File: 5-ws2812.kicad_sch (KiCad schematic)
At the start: 5 parts

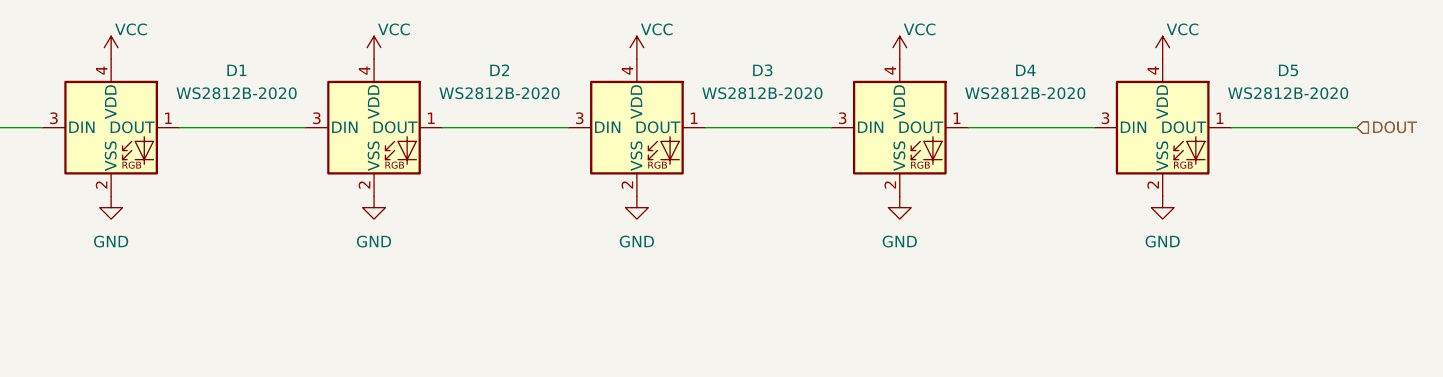
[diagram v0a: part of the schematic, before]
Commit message: Added front artwork and token on the back
Also:
- Tweaked the trace to the antenna to hopefully better match 50ohm impedance
- Tweaked all traces to use fillet on all corners
- Added/fixed parts information

Signed-off-by: Thomas Flummer <tf@flummer.net>
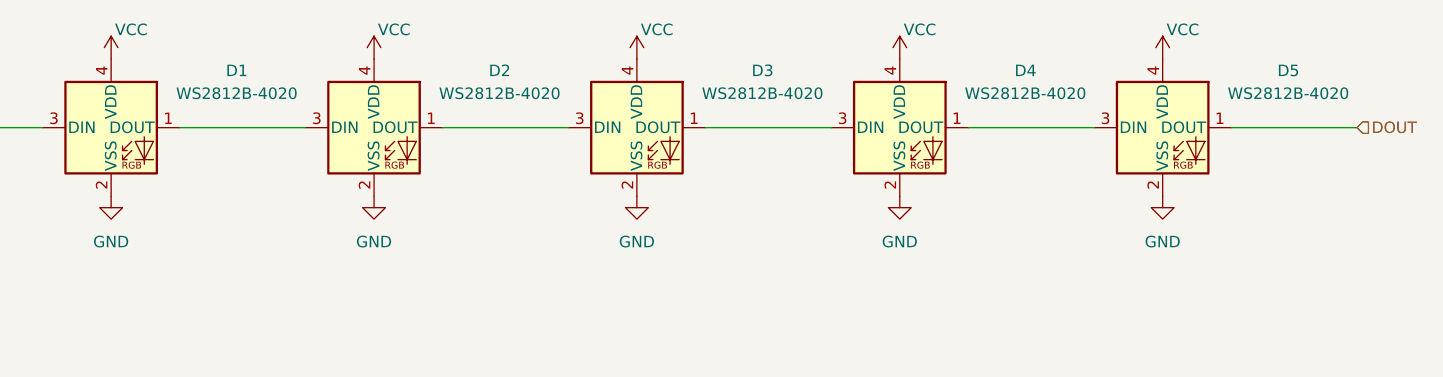
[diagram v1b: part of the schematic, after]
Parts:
- D1, D2, D3, D4, D5: value WS2812B-2020 -> WS2812B-4020; LCSC (none) -> C965557
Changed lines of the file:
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@@
 			)
 		)
-		(property "Value" "WS2812B-2020"
+		(property "Value" "WS2812B-4020"
 			(at 116.84 73.6914 0)
 			(effects
@@
 		)
 		(property "Description" "RGB LED with integrated controller, 2.0 x 2.0 mm, 12 mA"
+			(at 102.87 77.47 0)
+			(effects
+				(font
+					(size 1.27 1.27)
+				)
+				(hide yes)
+			)
+		)
+		(property "LCSC" "C965557"
 			(at 102.87 77.47 0)
 			(effects
@@
 			)
 		)
-		(property "Value" "WS2812B-2020"
+		(property "Value" "WS2812B-4020"
 			(at 175.26 73.6914 0)
 			(effects
@@
 		)
 		(property "Description" "RGB LED with integrated controller, 2.0 x 2.0 mm, 12 mA"
+			(at 161.29 77.47 0)
+			(effects
+				(font
+					(size 1.27 1.27)
+				)
+				(hide yes)
+			)
+		)
+		(property "LCSC" "C965557"
 			(at 161.29 77.47 0)
 			(effects
@@
 			)
 		)
-		(property "Value" "WS2812B-2020"
+		(property "Value" "WS2812B-4020"
 			(at 233.68 73.6914 0)
 			(effects
@@
 		)
 		(property "Description" "RGB LED with integrated controller, 2.0 x 2.0 mm, 12 mA"
+			(at 219.71 77.47 0)
+			(effects
+				(font
+					(size 1.27 1.27)
+				)
+				(hide yes)
+			)
+		)
+		(property "LCSC" "C965557"
 			(at 219.71 77.47 0)
 			(effects
@@
 			)
 		)
-		(property "Value" "WS2812B-2020"
+		(property "Value" "WS2812B-4020"
 			(at 204.47 73.6914 0)
 			(effects
@@
 		)
 		(property "Description" "RGB LED with integrated controller, 2.0 x 2.0 mm, 12 mA"
+			(at 190.5 77.47 0)
+			(effects
+				(font
+					(size 1.27 1.27)
+				)
+				(hide yes)
+			)
+		)
+		(property "LCSC" "C965557"
 			(at 190.5 77.47 0)
 			(effects
@@
 			)
 		)
-		(property "Value" "WS2812B-2020"
+		(property "Value" "WS2812B-4020"
 			(at 146.05 73.6914 0)
 			(effects
@@
 			(at 132.08 77.47 0)
 			(effects
+				(font
+					(size 1.27 1.27)
+				)
+				(hide yes)
+			)
+		)
+		(property "LCSC" "C965557"
+			(at 132.08 77.47 0)
+			(effects
